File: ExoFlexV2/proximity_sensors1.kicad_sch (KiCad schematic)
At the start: 43 parts

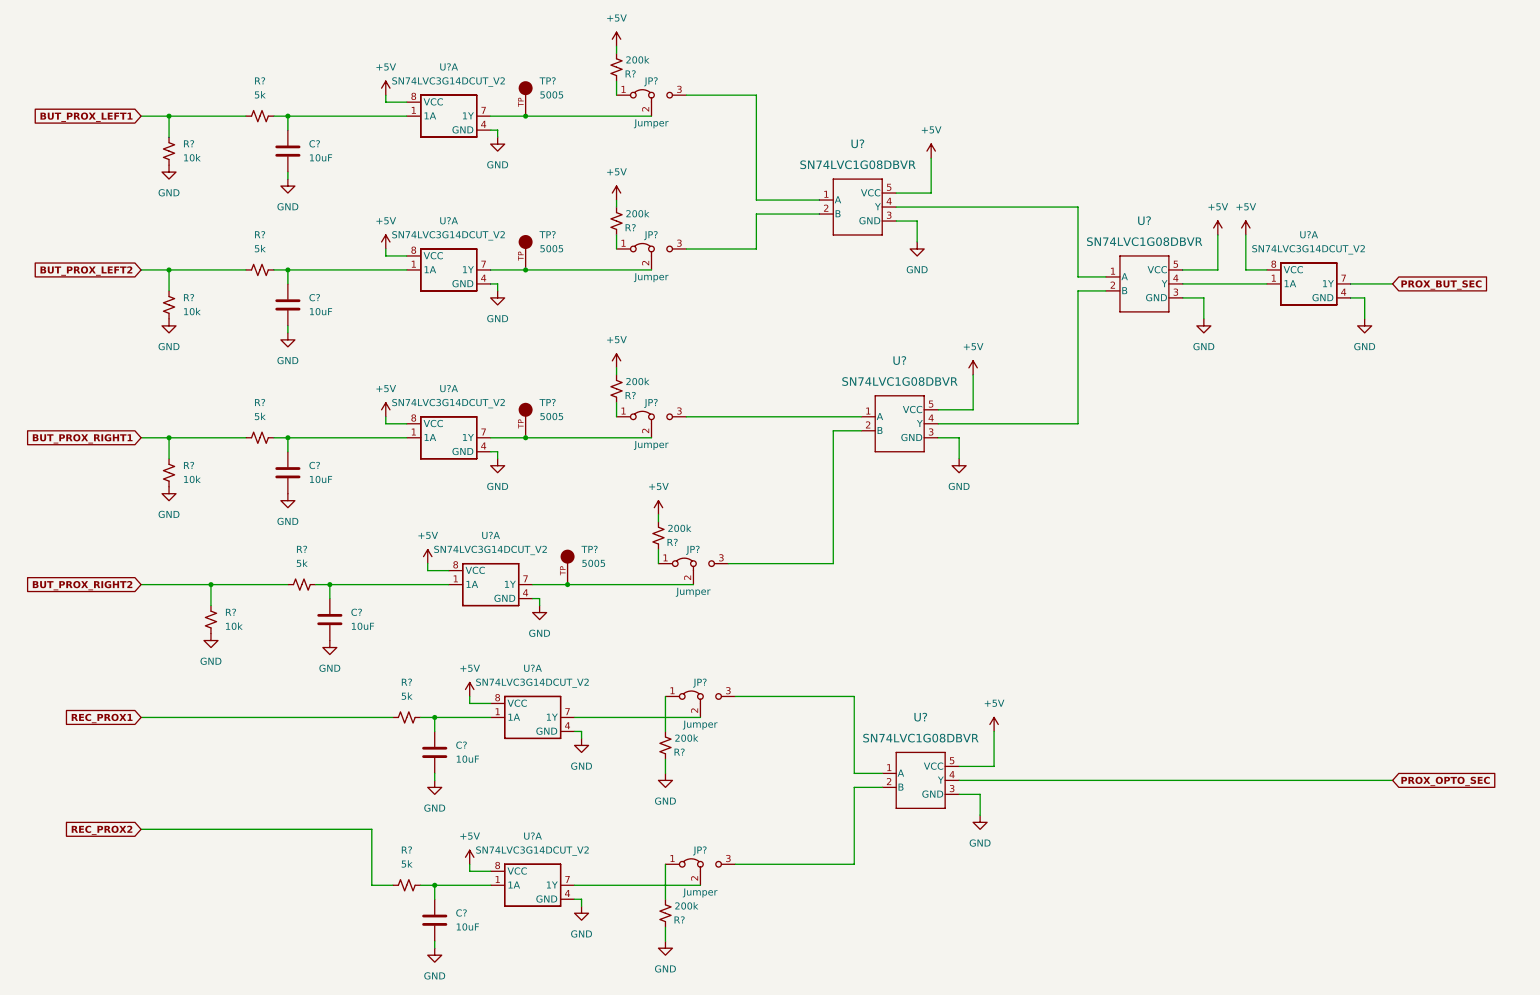
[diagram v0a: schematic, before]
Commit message: Mise à jour signaux STM
- Condo de découplage
- Signaux supplémentaire pour le STM
- Page GND sera pour Multiplexeur
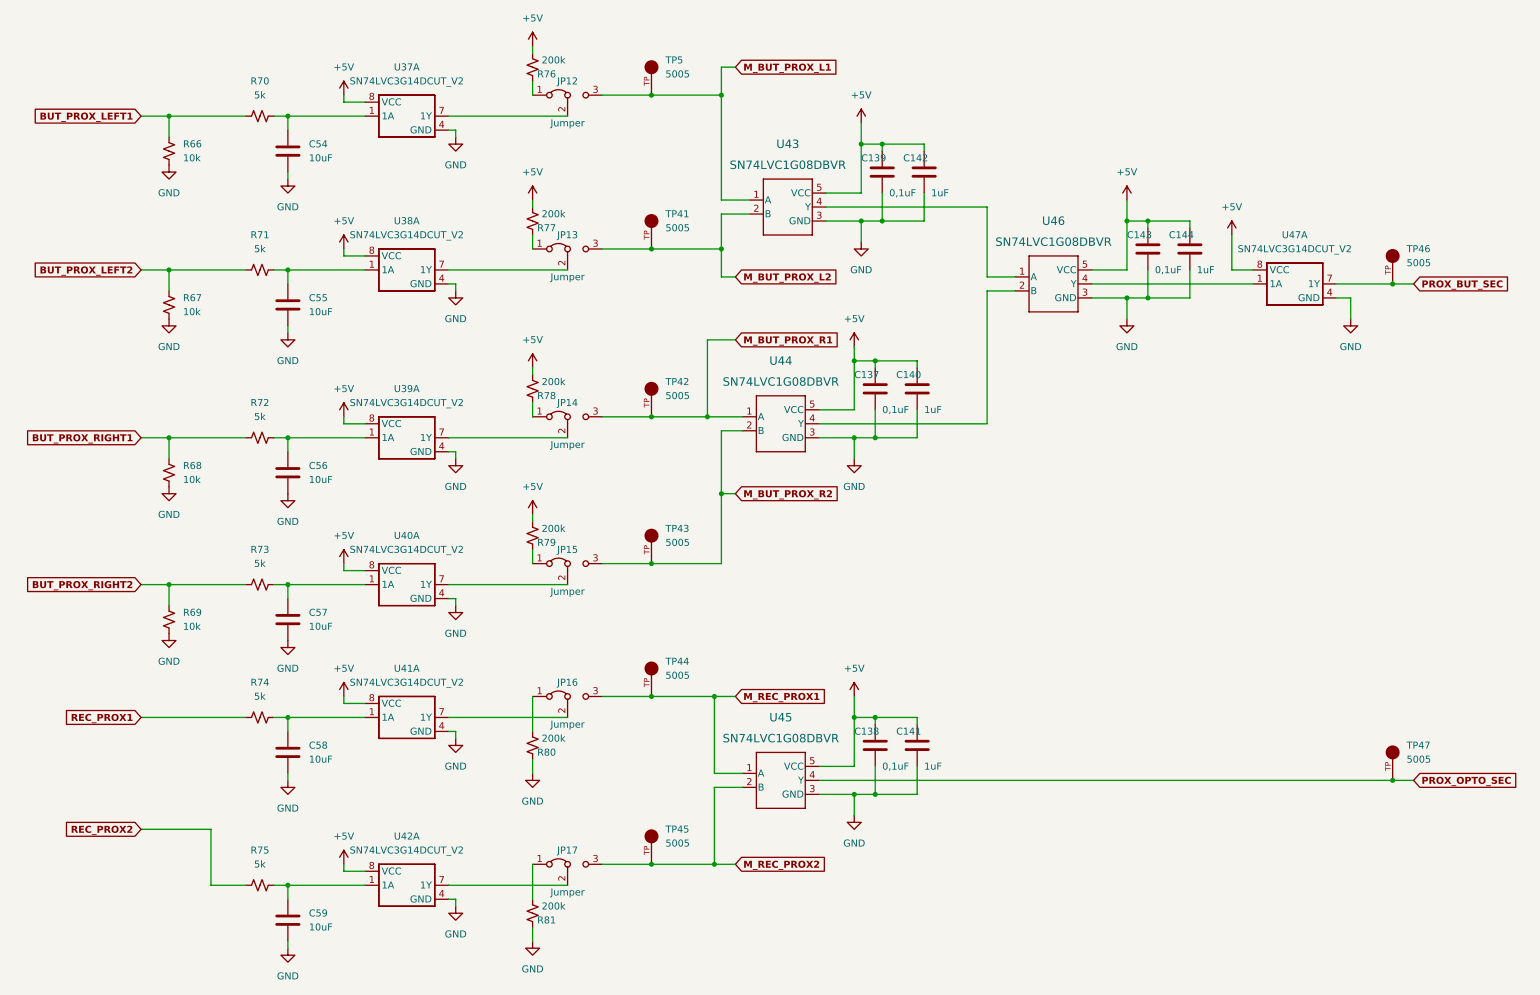
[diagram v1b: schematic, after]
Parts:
- removed TP? (x4): 5005, FootPrint:KEYSTONE_5005, symbol SymLib:5005
- added C137, C138, C139, C143: 0,1uF, Capacitor_SMD:C_0603_1608Metric, symbol Device:C
- added C140, C141, C142, C144: 1uF, Capacitor_SMD:C_0603_1608Metric, symbol Device:C
- added TP41, TP42, TP43, TP44, TP45, TP46, TP47, TP5: 5005, FootPrint:KEYSTONE_5005, symbol SymLib:5005
- gave numbers to parts that had none: 39
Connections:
- net +5V: now also C137.1, C138.1, C139.1, C140.1, C141.1, C142.1, C143.1, C144.1
- net GND: now also C137.2, C138.2, C139.2, C140.2, C141.2, C142.2, C143.2, C144.2
- net PROX_BUT_SEC: now also TP46.TP
- net PROX_OPTO_SEC: now also TP47.TP
- net M_BUT_PROX_L1: now reaches JP12.3 (B), U43.1 (A)
- net M_BUT_PROX_L1: now also TP5.TP
- net M_BUT_PROX_L2: now reaches JP13.3 (B), U43.2 (B)
- net M_BUT_PROX_L2: now also TP41.TP
- net M_REC_PROX1: now reaches JP16.3 (B), U45.1 (A)
- net M_REC_PROX1: now also TP44.TP
- net M_REC_PROX2: now reaches JP17.3 (B), U45.2 (B)
- net M_REC_PROX2: now also TP45.TP
- net M_BUT_PROX_R1: now reaches JP14.3 (B), U44.1 (A)
- net M_BUT_PROX_R1: now also TP42.TP
- net M_BUT_PROX_R2: now reaches JP15.3 (B), U44.2 (B)
- net M_BUT_PROX_R2: now also TP43.TP
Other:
- moved on the sheet: C57, C58, C59, JP12, JP13, JP14, JP15, JP16, JP17, R69, R73, R74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

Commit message: Finalisation 1
- Ajout de pages pour la gestion des signaux négatif
- Modification des pages de torque et amplitude
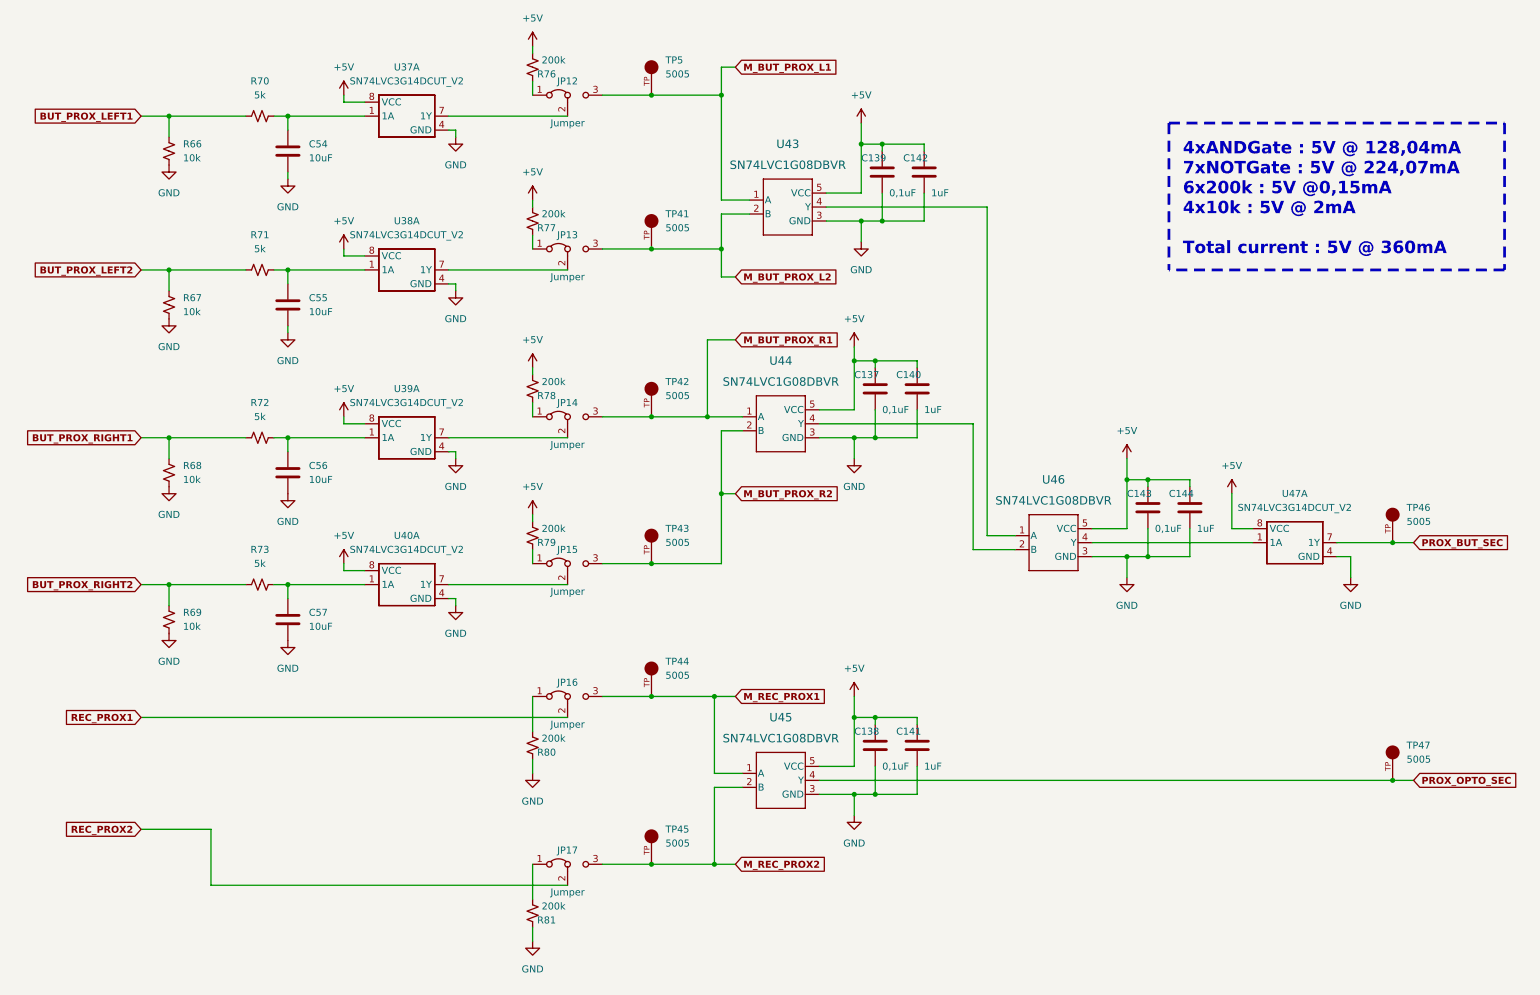
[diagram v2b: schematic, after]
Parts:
- removed C58, C59: 10uF, Capacitor_SMD:C_0603_1608Metric, symbol Device:C
- removed R74, R75: 5k, Resistor_SMD:R_0603_1608Metric, symbol Device:R_Small_US
- removed U41, U42: SN74LVC3G14DCUT_V2, FootPrint:SN74LVC3G14DCUT, symbol SymLib:SN74LVC3G14DCUT_V2
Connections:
- net REC_PROX1: now also JP16.2 (C)
- net REC_PROX2: now also JP17.2 (C)
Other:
- note added: "4xANDGate : 5V @ 128,04mA 7xNOTGate : 5V @ 224,07mA 6x200k : 5V @0,15mA 4x10k : 5V @ 2mA Total current : 5V @ 360mA"
- moved on the sheet: C143, C144, TP46, U46, U47A
